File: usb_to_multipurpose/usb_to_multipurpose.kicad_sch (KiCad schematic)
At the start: 33 parts, among them U1 FT232H, U2 AP2112K-3.3TRG1, U5 93LC56BT-I/OT, Y1 12MHz

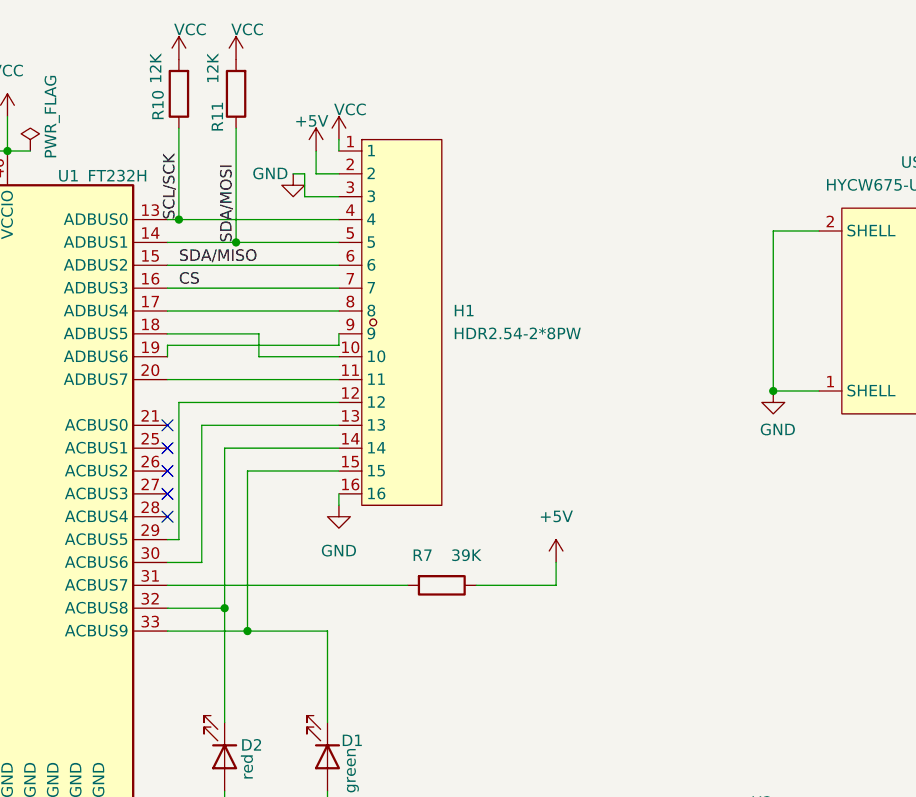
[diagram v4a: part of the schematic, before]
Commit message: Change connector for smaller JST SH 2x6 pin.
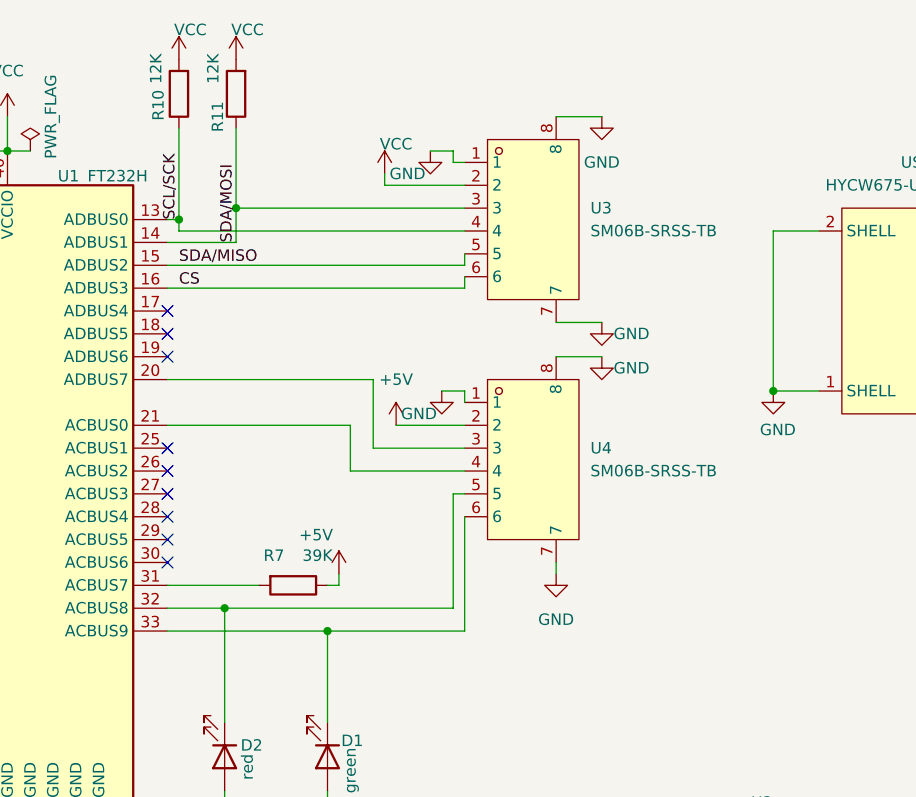
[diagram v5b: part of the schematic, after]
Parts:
- removed H1: HDR2.54-2*8PW, easyeda2kicad:HDR-TH_16P-P2.54-H-F-R2-C8-S2.54-W10.0, symbol easyeda2kicad:HDR2.54-2*8PW
- added U3, U4: SM06B-SRSS-TB, easyeda2kicad:CONN-SMD_SM06B-SRSS-TB-LF-SN, symbol easyeda2kicad:SM06B-SRSS-TB
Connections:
- net +5V: now also U4.2
- net CS: now also U3.6
- net GND: now also U3.1, U3.7, U3.8, U4.1, U4.7, U4.8
- net SCL/SCK: now also U3.4
- net SDA/MISO: now also U3.5
- net SDA/MOSI: now also U3.3
- net VCC: now also U3.2
- net at U1.20 (ADBUS7): now also U4.3
- net at U1.21 (ACBUS0): now also U4.4
- net at D2.1 (K), U1.32 (ACBUS8): now also U4.5
- net at D1.1 (K), U1.33 (ACBUS9): now also U4.6
- no-connect marks 6 -> 10
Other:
- moved on the sheet: R7

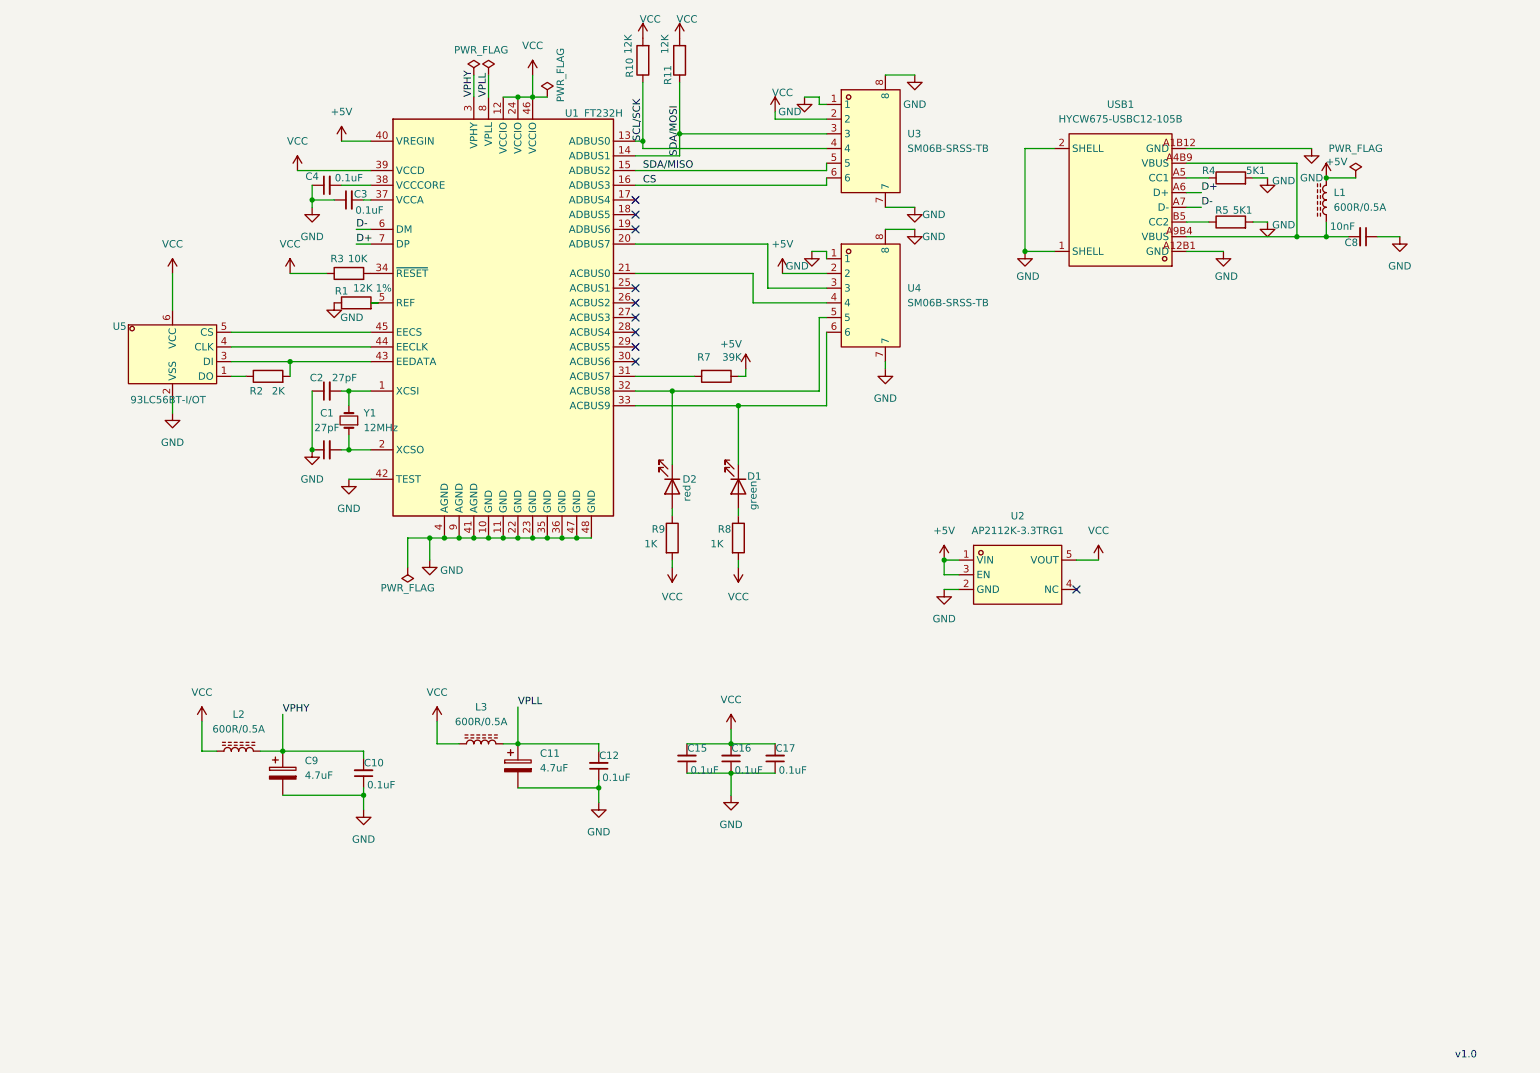
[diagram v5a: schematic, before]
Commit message: Add comments and improve readability of the schematic
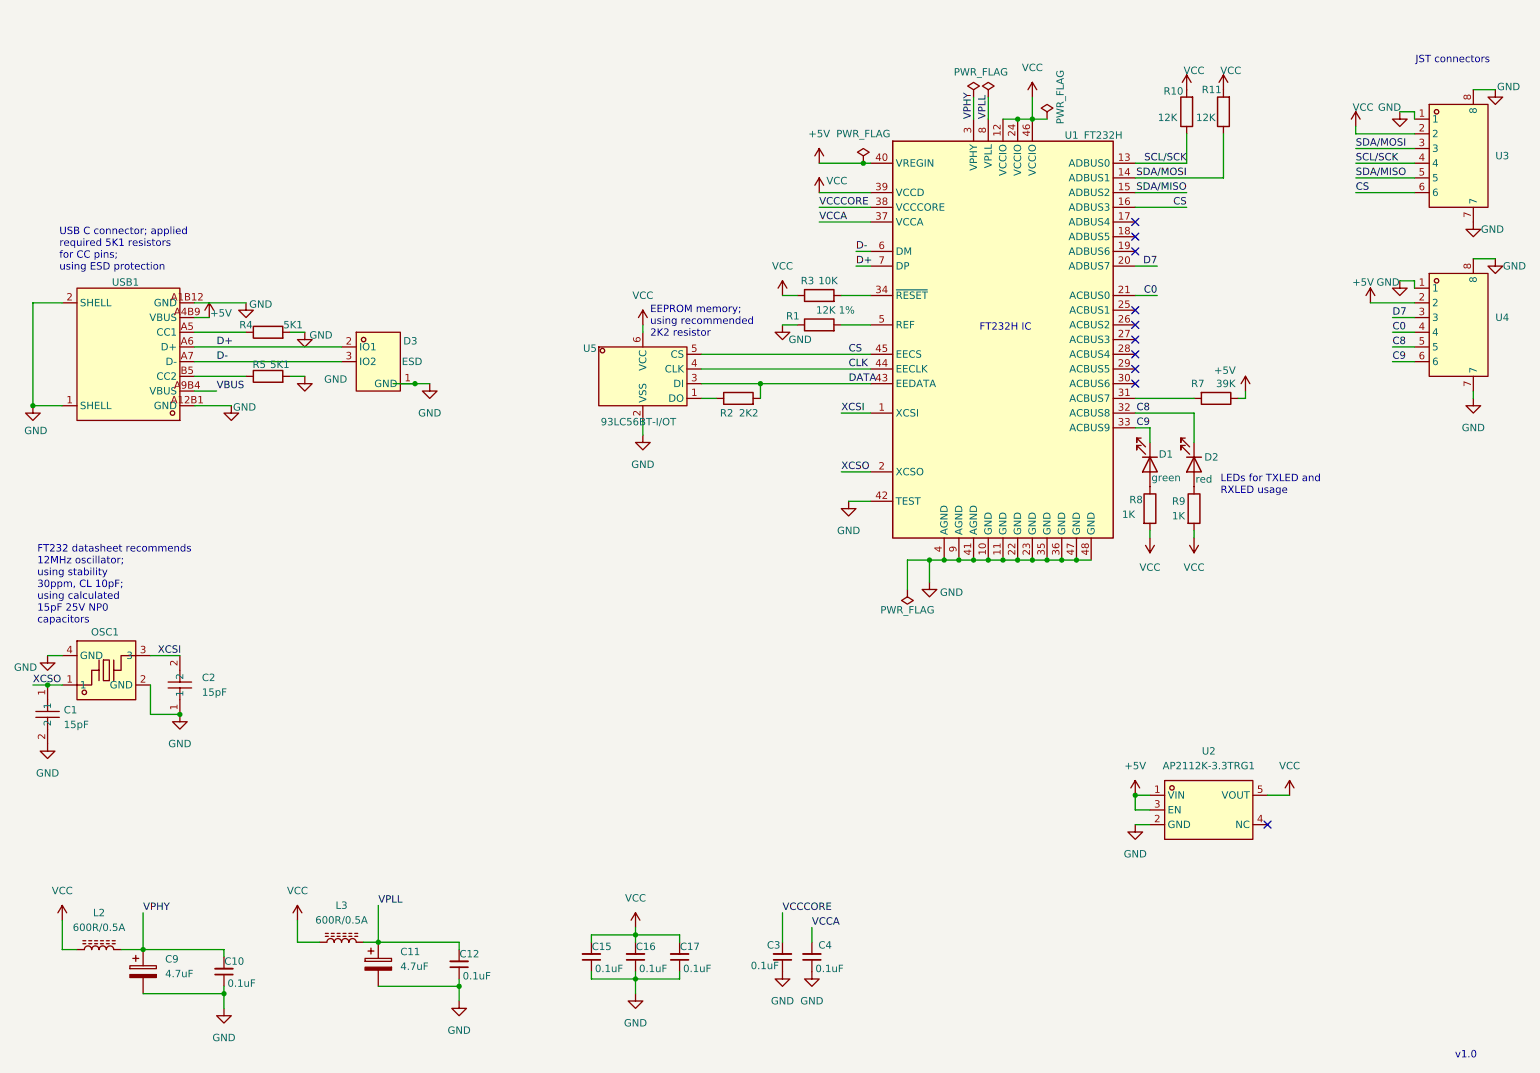
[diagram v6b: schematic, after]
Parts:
- removed C1, C2: 27pF, easyeda2kicad:C0402, symbol Device:C_Small
- removed C8: 10nF, easyeda2kicad:C0201, symbol Device:C_Small
- removed L1: 600R/0.5A, easyeda2kicad:L0805, symbol Device:L_Ferrite
- removed Y1: 12MHz, easyeda2kicad:OSC-SMD_4P-L3.2-W2.5-BL, symbol Device:Crystal_Small
- added C1, C2: 15pF, easyeda2kicad:C0201, symbol easyeda2kicad:0201N150J250CT
- added D3: ESD, easyeda2kicad:X2SON-3_L1.3-W0.6-L, symbol easyeda2kicad:ESD122DMYR
- added OSC1: TX322512M4DBDE2T, easyeda2kicad:OSC-SMD_4P-L3.2-W2.5-BL, symbol easyeda2kicad:TX322512M4DBDE2T
- R2: value 2K -> 2K2
- U3, U4: value SM06B-SRSS-TB -> JST connector
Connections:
- net +5V: now also USB1.A4B9 (VBUS)
- net CS: now also U1.45 (EECS), U5.5 (CS)
- net D+: now also D3.2 (IO1)
- net D-: now also D3.3 (IO2)
- net GND: now also C1.2, C2.1, D3.1 (GND), OSC1.2 (GND), OSC1.4 (GND)
- net DATA: now reaches R2.2, U1.43 (EEDATA), U5.3 (DI)
- net CLK: now reaches U1.44 (EECLK), U5.4 (CLK)
- net XCSI: now reaches U1.1 (XCSI)
- net XCSI: now also C2.2, OSC1.3
- net XCSO: now reaches U1.2 (XCSO)
- net XCSO: now also C1.1, OSC1.1
- net D7: now reaches U1.20 (ADBUS7), U4.3
- net C0: now reaches U1.21 (ACBUS0), U4.4
- net C8: now reaches D2.1 (K), U1.32 (ACBUS8), U4.5
- net C9: now reaches D1.1 (K), U1.33 (ACBUS9), U4.6
- net VCCA: now reaches U1.37 (VCCA)
- net VCCA: now also C4.2; no longer C3.2
- net VCCCORE: now reaches U1.38 (VCCCORE)
- net VCCCORE: now also C3.2; no longer C4.2
- net VBUS: now reaches USB1.A9B4 (VBUS)
- net VBUS: no longer USB1.A4B9 (VBUS)
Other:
- note added: "EEPROM memory; using recommended 2K2 resistor"
- note added: "FT232 datasheet recommends 12MHz oscillator; using stability 30ppm, CL 10pF; using calculated 15pF 25V NP0 capacitors"
- note added: "FT232H IC"
- note added: "JST connectors"
- note added: "LEDs for TXLED and RXLED usage"
- note added: "USB C connector; applied required 5K1 resistors for CC pins; using ESD protection"
- moved on the sheet: C10, C11, C12, C15, C16, C17, C3, C4, C9, D1, D2, L2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
